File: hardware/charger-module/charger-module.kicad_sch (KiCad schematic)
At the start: 72 parts, among them J1 Bus_PCI_Express_x1, J2 Conn_01x06_Pin, J3 RP_USB, J4 USB_C_Receptacle_USB2.0_14P, SW1 BOOT, SW2 RESET, U1 AMS1117-3.3, U2 W25Q32JVSSIQ, U3 RP2040, U4 MPQ4242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

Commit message: chore: add jlcpcb component part number
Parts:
- U5: LCSC (none) -> C265125
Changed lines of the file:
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@@
+			)
+		)
+		(property "LCSC" "C265125"
+			(at 293.37 198.12 0)
+			(effects
+				(font
+					(size 1.27 1.27)
+				)
+				(hide yes)
 			)
 		)

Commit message: chore: add tweaks for production
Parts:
- U5: JLCPCB_CORRECTION (none) -> 0;0;180
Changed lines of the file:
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@@
+			)
+		)
+		(property "JLCPCB_CORRECTION" "0;0;180"
+			(at 293.37 198.12 0)
+			(effects
+				(font
+					(size 1.27 1.27)
+				)
+				(hide yes)
 			)
 		)

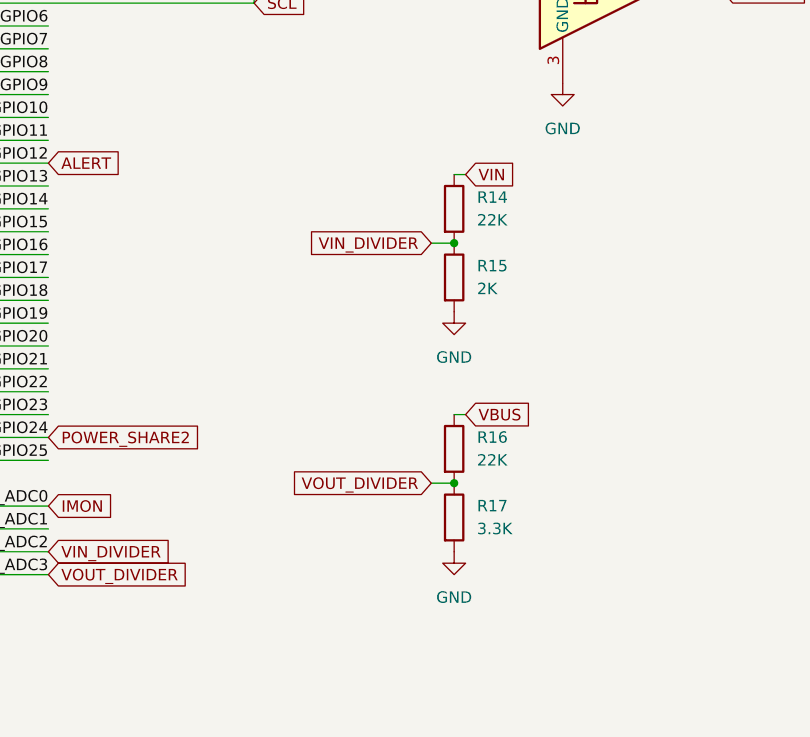
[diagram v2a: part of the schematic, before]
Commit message: fix: reference vout voltage divider to gndusb for accuracy
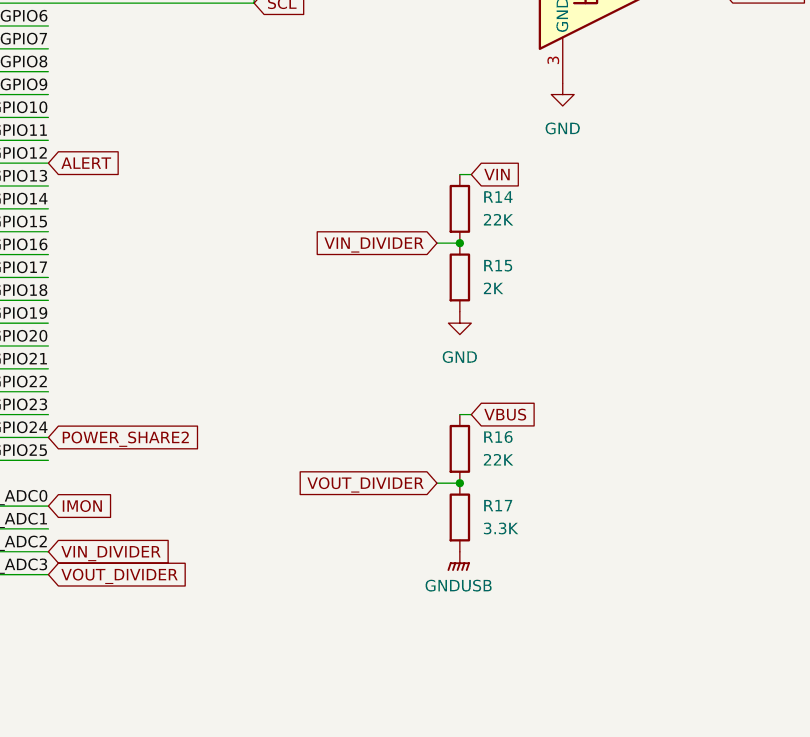
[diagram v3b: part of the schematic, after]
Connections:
- net GND: no longer R17.2
- net GNDUSB: now also R17.2
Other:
- moved on the sheet: R14, R15, R16, R17
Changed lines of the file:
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@@
 	)
 	(junction
-		(at 276.225 226.06)
+		(at 276.86 226.06)
 		(diameter 0)
 		(color 0 0 0 0)
@@
 	)
 	(junction
-		(at 276.225 252.73)
+		(at 276.86 252.73)
 		(diameter 0)
 		(color 0 0 0 0)
@@
 	(wire
 		(pts
-			(xy 277.495 218.44) (xy 276.225 218.44)
+			(xy 278.13 218.44) (xy 276.86 218.44)
 		)
 		(stroke
@@
 	(wire
 		(pts
-			(xy 277.495 245.11) (xy 276.225 245.11)
+			(xy 278.13 245.11) (xy 276.86 245.11)
 		)
 		(stroke
@@
 	(wire
 		(pts
-			(xy 273.685 252.73) (xy 276.225 252.73)
+			(xy 274.32 252.73) (xy 276.86 252.73)
 		)
 		(stroke
@@
 	(wire
 		(pts
-			(xy 273.685 226.06) (xy 276.225 226.06)
+			(xy 274.32 226.06) (xy 276.86 226.06)
 		)
 		(stroke
@@
 	(global_label "VBUS"
 		(shape input)
-		(at 277.495 245.11 0)
+		(at 278.13 245.11 0)
 		(fields_autoplaced yes)
 		(effects
@@
 		)
 		(property "Intersheetrefs" "${INTERSHEET_REFS}"
-			(at 285.3788 245.11 0)
+			(at 286.0138 245.11 0)
 			(effects
 				(font
@@
 	(global_label "VIN"
 		(shape input)
-		(at 277.495 218.44 0)
+		(at 278.13 218.44 0)
 		(fields_autoplaced yes)
 		(effects
@@
 		)
 		(property "Intersheetrefs" "${INTERSHEET_REFS}"
-			(at 283.5041 218.44 0)
+			(at 284.1391 218.44 0)
 			(effects
 				(font
@@
 	(global_label "VOUT_DIVIDER"
 		(shape input)
-		(at 273.685 252.73 180)
+		(at 274.32 252.73 180)
 		(fields_autoplaced yes)
 		(effects
@@
 		)
 		(property "Intersheetrefs" "${INTERSHEET_REFS}"
-			(at 257.7578 252.73 0)
+			(at 258.3928 252.73 0)
 			(effects
 				(font
@@
 	(global_label "VIN_DIVIDER"
 		(shape input)
-		(at 273.685 226.06 180)
+		(at 274.32 226.06 180)
 		(fields_autoplaced yes)
 		(effects
@@
 		)
 		(property "Intersheetrefs" "${INTERSHEET_REFS}"
-			(at 259.4511 226.06 0)
+			(at 260.0861 226.06 0)
 			(effects
 				(font
@@
 	(symbol
 		(lib_id "Device:R")
-		(at 276.225 248.92 0)
+		(at 276.86 248.92 0)
 		(unit 1)
 		(exclude_from_sim no)
@@
 		(fields_autoplaced yes)
 		(property "Reference" "R16"
-			(at 278.765 247.6499 0)
+			(at 279.4 247.6499 0)
 			(effects
 				(font
@@
 		)
 		(property "Value" "22K"
-			(at 278.765 250.1899 0)
+			(at 279.4 250.1899 0)
 			(effects
 				(font
@@
 		)
 		(property "Footprint" "Resistor_SMD:R_0402_1005Metric"
-			(at 274.447 248.92 90)
+			(at 275.082 248.92 90)
 			(effects
 				(font
@@
 		)
 		(property "Datasheet" "~"
-			(at 276.225 248.92 0)
+			(at 276.86 248.92 0)
 			(effects
 				(font
@@
 		)
 		(property "Description" "Resistor"
-			(at 276.225 248.92 0)
+			(at 276.86 248.92 0)
 			(effects
 				(font
@@
 		)
 		(property "LCSC" "C25768"
-			(at 276.225 248.92 0)
+			(at 276.86 248.92 0)
 			(effects
 				(font
@@
 		(lib_name "GND_1")
 		(lib_id "power:GND")
-		(at 276.225 233.68 0)
+		(at 276.86 233.68 0)
 		(unit 1)
 		(exclude_from_sim no)
@@
 		(fields_autoplaced yes)
 		(property "Reference" "#PWR034"
-			(at 276.225 240.03 0)
+			(at 276.86 240.03 0)
 			(effects
 				(font
@@
 		)
 		(property "Value" "GND"
-			(at 276.225 238.76 0)
+			(at 276.86 238.76 0)
 			(effects
 				(font
@@
 		)
 		(property "Footprint" ""
-			(at 276.225 233.68 0)
+			(at 276.86 233.68 0)
 			(effects
 				(font
@@
 		)
 		(property "Datasheet" ""
-			(at 276.225 233.68 0)
+			(at 276.86 233.68 0)
 			(effects
 				(font
@@
 		)
 		(property "Description" "Power symbol creates a global label with name \"GND\" , ground"
-			(at 276.225 233.68 0)
+			(at 276.86 233.68 0)
 			(effects
 				(font
@@
 	)
 	(symbol
-		(lib_name "GND_1")
-		(lib_id "power:GND")
-		(at 276.225 260.35 0)
-		(unit 1)
-		(exclude_from_sim no)
-		(in_bom yes)
-		(on_board yes)
-		(dnp no)
-		(fields_autoplaced yes)
-		(property "Reference" "#PWR035"
-			(at 276.225 266.7 0)
-			(effects
-				(font
-					(size 1.27 1.27)
-				)
-				(hide yes)
-			)
-		)
-		(property "Value" "GND"
-			(at 276.225 265.43 0)
-			(effects
-				(font
-					(size 1.27 1.27)
-				)
-			)
-		)
-		(property "Footprint" ""
-			(at 276.225 260.35 0)
-			(effects
-				(font
-					(size 1.27 1.27)
-				)
-				(hide yes)
-			)
-		)
-		(property "Datasheet" ""
-			(at 276.225 260.35 0)
-			(effects
-				(font
-					(size 1.27 1.27)
-				)
-				(hide yes)
-			)
-		)
-		(property "Description" "Power symbol creates a global label with name \"GND\" , ground"
-			(at 276.225 260.35 0)
-			(effects
-				(font
-					(size 1.27 1.27)
-				)
-				(hide yes)
-			)
-		)
-		(pin "1"
-		)
-		(instances
-			(project "charger-module"
-				(path "/ab392f3e-5179-4380-b283-87f14bada4d4"
-					(reference "#PWR035")
-					(unit 1)
-				)
-			)
-		)
-	)
-	(symbol
 		(lib_id "power:GND")
 		(at 154.94 161.29 0)
@@
 	)
 	(symbol
+		(lib_id "power:GNDPWR")
+		(at 276.86 260.35 0)
+		(unit 1)
+		(exclude_from_sim no)
+		(in_bom yes)
+		(on_board yes)
+		(dnp no)
+		(fields_autoplaced yes)
+		(property "Reference" "#PWR048"
+			(at 276.86 265.43 0)
+			(effects
+				(font
+					(size 1.27 1.27)
+				)
+				(hide yes)
+			)
+		)
+		(property "Value" "GNDUSB"
+			(at 276.733 264.16 0)
+			(effects
+				(font
+					(size 1.27 1.27)
+				)
+			)
+		)
+		(property "Footprint" ""
+			(at 276.86 261.62 0)
+			(effects
+				(font
+					(size 1.27 1.27)
+				)
+				(hide yes)
+			)
+		)
+		(property "Datasheet" ""
+			(at 276.86 261.62 0)
+			(effects
+				(font
+					(size 1.27 1.27)
+				)
+				(hide yes)
+			)
+		)
+		(property "Description" "Power symbol creates a global label with name \"GNDPWR\" , global ground"
+			(at 276.86 260.35 0)
+			(effects
+				(font
+					(size 1.27 1.27)
+				)
+				(hide yes)
+			)
+		)
+		(pin "1"
+		)
+		(instances
+			(project "charger-module"
+				(path "/ab392f3e-5179-4380-b283-87f14bada4d4"
+					(reference "#PWR048")
+					(unit 1)
+				)
+			)
+		)
+	)
+	(symbol
 		(lib_id "Switch:SW_Push")
 		(at 44.45 203.2 0)
@@
 	(symbol
 		(lib_id "Device:R")
-		(at 276.225 222.25 0)
+		(at 276.86 222.25 0)
 		(unit 1)
 		(exclude_from_sim no)
@@
 		(fields_autoplaced yes)
 		(property "Reference" "R14"
-			(at 278.765 220.9799 0)
+			(at 279.4 220.9799 0)
 			(effects
 				(font
@@
 		)
 		(property "Value" "22K"
-			(at 278.765 223.5199 0)
+			(at 279.4 223.5199 0)
 			(effects
 				(font
@@
 		)
 		(property "Footprint" "Resistor_SMD:R_0402_1005Metric"
-			(at 274.447 222.25 90)
+			(at 275.082 222.25 90)
 			(effects
 				(font
@@
 		)
 		(property "Datasheet" "~"
-			(at 276.225 222.25 0)
+			(at 276.86 222.25 0)
 			(effects
 				(font
@@
 		)
 		(property "Description" "Resistor"
-			(at 276.225 222.25 0)
+			(at 276.86 222.25 0)
 			(effects
 				(font
@@
 		)
 		(property "LCSC" "C25768"
-			(at 276.225 222.25 0)
+			(at 276.86 222.25 0)
 			(effects
 				(font
@@
 	(symbol
 		(lib_id "Device:R")
-		(at 276.225 256.54 0)
+		(at 276.86 256.54 0)
 		(unit 1)
 		(exclude_from_sim no)
@@
 		(fields_autoplaced yes)
 		(property "Reference" "R17"
-			(at 278.765 255.2699 0)
+			(at 279.4 255.2699 0)
 			(effects
 				(font
@@
 		)
 		(property "Value" "3.3K"
-			(at 278.765 257.8099 0)
+			(at 279.4 257.8099 0)
 			(effects
 				(font
@@
 		)
 		(property "Footprint" "Resistor_SMD:R_0402_1005Metric"
-			(at 274.447 256.54 90)
+			(at 275.082 256.54 90)
 			(effects
 				(font
@@
 		)
 		(property "Datasheet" "~"
-			(at 276.225 256.54 0)
+			(at 276.86 256.54 0)
 			(effects
 				(font
@@
 		)
 		(property "Description" "Resistor"
-			(at 276.225 256.54 0)
+			(at 276.86 256.54 0)
 			(effects
 				(font
@@
 		)
 		(property "LCSC" "C25890"
-			(at 276.225 256.54 0)
+			(at 276.86 256.54 0)
 			(effects
 				(font
@@
 	(symbol
 		(lib_id "Device:R")
-		(at 276.225 229.87 0)
+		(at 276.86 229.87 0)
 		(unit 1)
 		(exclude_from_sim no)
@@
 		(fields_autoplaced yes)
 		(property "Reference" "R15"
-			(at 278.765 228.5999 0)
+			(at 279.4 228.5999 0)
 			(effects
 				(font
@@
 		)
 		(property "Value" "2K"
-			(at 278.765 231.1399 0)
+			(at 279.4 231.1399 0)
 			(effects
 				(font
@@
 		)
 		(property "Footprint" "Resistor_SMD:R_0402_1005Metric"
-			(at 274.447 229.87 90)
+			(at 275.082 229.87 90)
 			(effects
 				(font
@@
 		)
 		(property "Datasheet" "~"
-			(at 276.225 229.87 0)
+			(at 276.86 229.87 0)
 			(effects
 				(font
@@
 		)
 		(property "Description" "Resistor"
-			(at 276.225 229.87 0)
+			(at 276.86 229.87 0)
 			(effects
 				(font
@@
 		)
 		(property "LCSC" "C4109"
-			(at 276.225 229.87 0)
+			(at 276.86 229.87 0)
 			(effects
 				(font
